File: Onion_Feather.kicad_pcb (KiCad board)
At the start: 4 copper layers, 59.7 x 53.3 mm, 65 parts, among them IC1 MAX11646EUA+T, IC2 SN74HC367PWR, J1 HR911105A, J2 CON_HEADER_PRG_AVR_ICSP-PTH, J3 Conn_01x02, J4 USB_A, J5 M04PTH, U1 ONION-OMEGA2, U2 AP1117-33, U3 CP2102N-A01-GQFN24, U4 BQ25895RTW, U5 STF202-22T1G

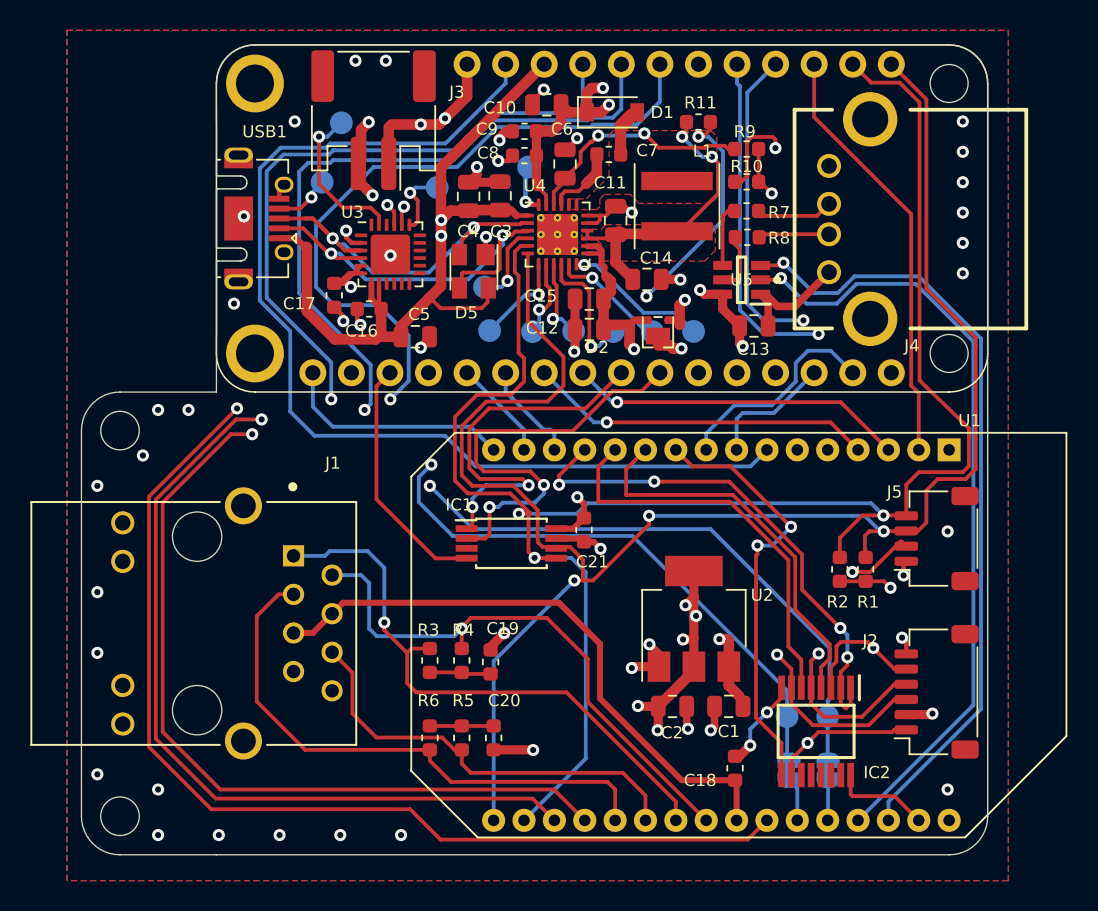
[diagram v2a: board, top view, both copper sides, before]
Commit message: #8 Re-route USB filter
Signed-off-by: Tisham Dhar <whatnickd@gmail.com>
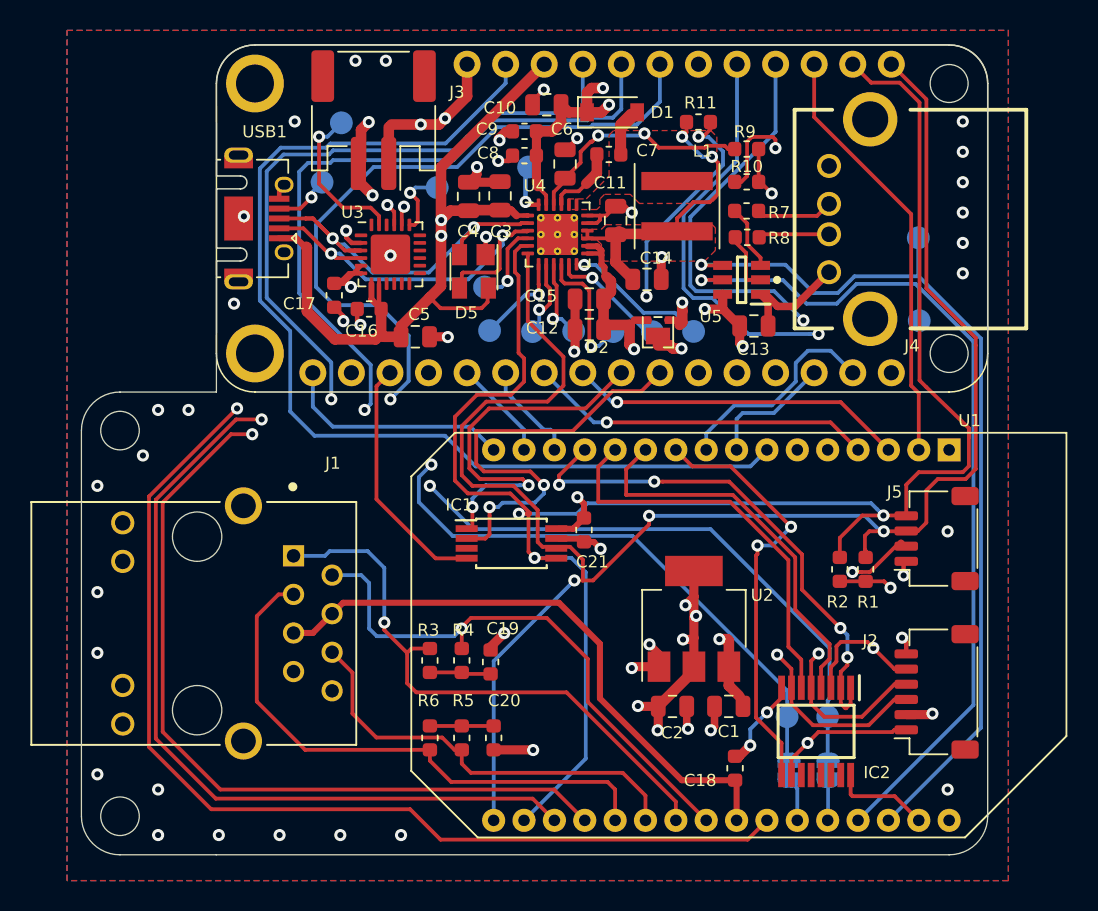
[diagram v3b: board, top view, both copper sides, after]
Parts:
- added TP14: TestPoint, TestPoint:TestPoint_Pad_D1.5mm, B.Cu at (163.1, 73.7)
- added TP15: TestPoint, TestPoint:TestPoint_Pad_D1.5mm, B.Cu at (163.1, 79.1)
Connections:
- U5 pad 2: USB_OUT- -> Net-(R8-Pad1)
- U5 pad 3: USB_OUT+ -> Net-(R7-Pad1)
- U5 pad 4: Net-(R7-Pad1) -> USB_OUT+
- U5 pad 5: Net-(R8-Pad1) -> USB_OUT-
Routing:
- net USB_OUT+: track 51.8 -> 59.6 mm
- net USB_OUT-: track 51.6 -> 59.3 mm
- net GPIO16: track 29.5 -> 34.1 mm
- net GPIO17: track 30.3 -> 34.6 mm
- net GND: track 64.0 -> 65.0 mm
- net VBAT: track 53.5 -> 52.9 mm
- net VIN: track 75.5 -> 75.0 mm

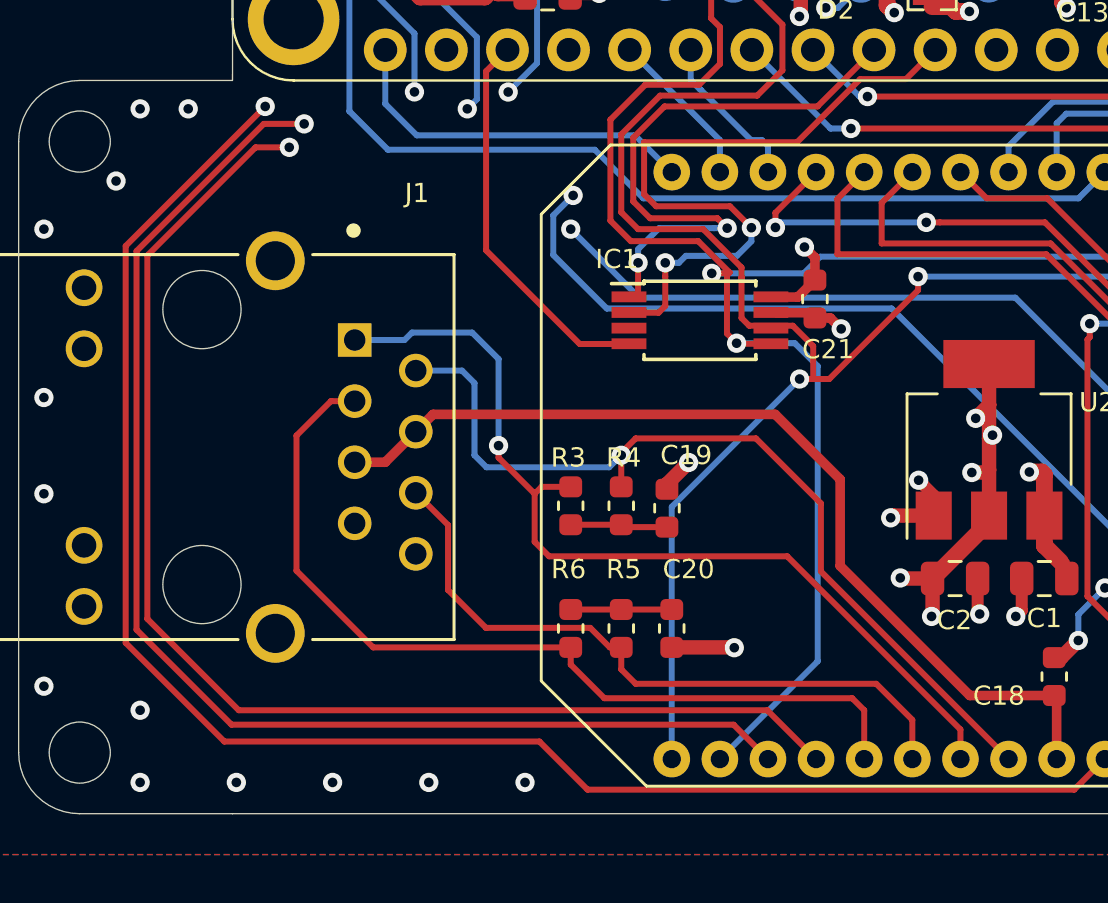
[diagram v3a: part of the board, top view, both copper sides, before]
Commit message: #9 Add some testpoints for ethernet
Signed-off-by: Tisham Dhar <whatnickd@gmail.com>
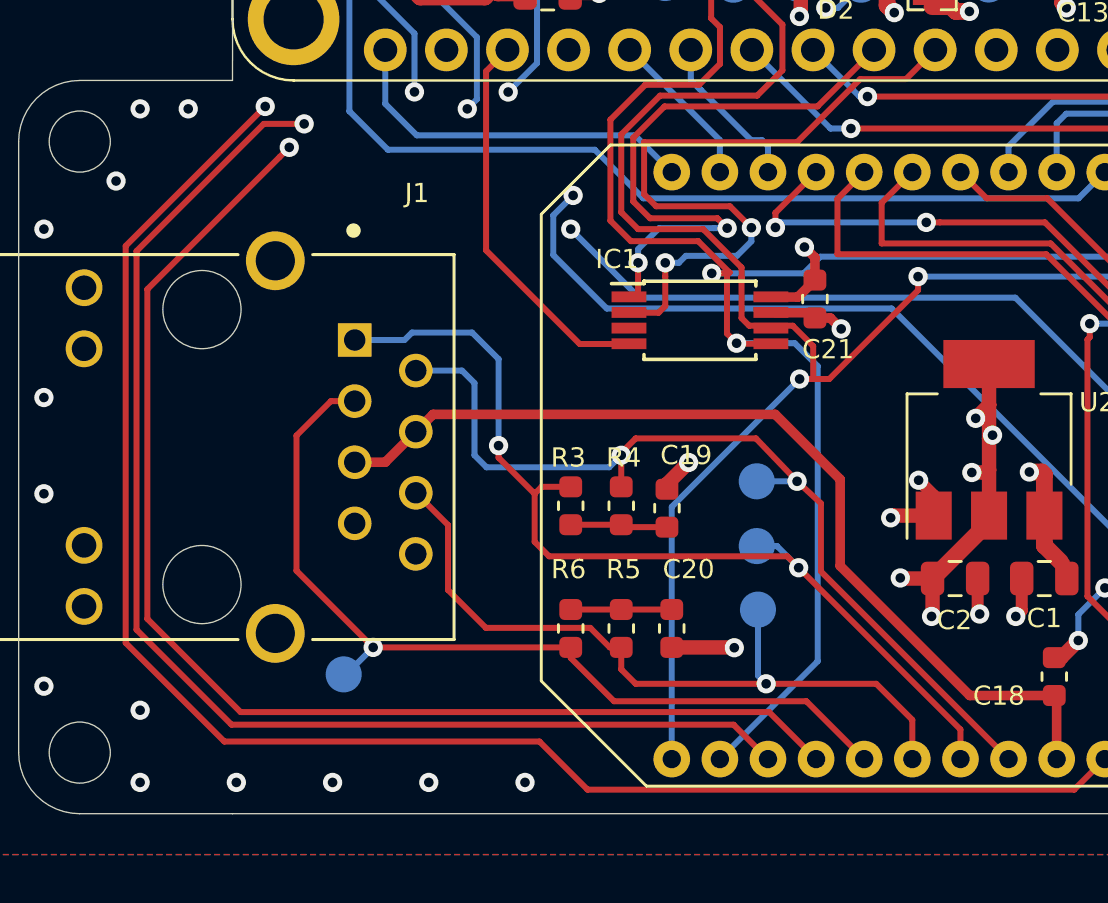
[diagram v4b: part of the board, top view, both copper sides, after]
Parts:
- added TP16: TestPoint, TestPoint:TestPoint_Pad_D1.5mm, B.Cu at (138.7, 105.8)
- added TP17: TestPoint, TestPoint:TestPoint_Pad_D1.5mm, B.Cu at (121.5, 108.5)
- added TP18: TestPoint, TestPoint:TestPoint_Pad_D1.5mm, B.Cu at (138.6, 100.5)
- added TP19: TestPoint, TestPoint:TestPoint_Pad_D1.5mm, B.Cu at (138.6, 103.2)
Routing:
- net ETH_RX-: track 28.3 -> 31.5 mm, vias 0 -> 1
- net ETH_TX+: track 38.6 -> 40.7 mm, vias 1 -> 2
- net ETH_TX-: track 37.1 -> 38.8 mm, vias 1 -> 2
- net GPIO18: track 104.8 -> 104.0 mm
- net ETH_RX+: track 37.1 -> 37.4 mm, vias 0 -> 1
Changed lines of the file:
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@@
     (thickness 1.6)
     (drawings 18)
-    (tracks 1120)
+    (tracks 1132)
     (zones 0)
-    (modules 67)
+    (modules 71)
     (nets 92)
   )
@@
   )
   (module TestPoint:TestPoint_Pad_D1.5mm (layer B.Cu)
+    (at 138.6332 103.1748)
+    (descr "SMD pad as test Point, diameter 1.5mm")
+    (tags "test point SMD pad")
+    (attr virtual)
+    (fp_text reference TP19 (at 3.4544 -0.0508) (layer B.SilkS)
+      (effects (font (size 1 1) (thickness 0.15)) (justify mirror))
+    )
+    (fp_text value TestPoint (at 0 -1.75) (layer B.Fab)
+      (effects (font (size 1 1) (thickness 0.15)) (justify mirror))
+    )
+    (fp_circle (center 0 0) (end 0 -0.95) (layer B.SilkS) (width 0.12))
+    (fp_circle (center 0 0) (end 1.25 0) (layer B.CrtYd) (width 0.05))
+    (fp_text user %R (at 0 1.65) (layer B.Fab)
+      (effects (font (size 1 1) (thickness 0.15)) (justify mirror))
+    )
+    (pad 1 smd circle (at 0 0) (size 1.5 1.5) (layers B.Cu B.Mask)
+      (net 30 ETH_TX+))
+  )
+  (module TestPoint:TestPoint_Pad_D1.5mm (layer B.Cu)
+    (at 138.6332 100.4824)
+    (descr "SMD pad as test Point, diameter 1.5mm")
+    (tags "test point SMD pad")
+    (attr virtual)
+    (fp_text reference TP18 (at 3.4036 0) (layer B.SilkS)
+      (effects (font (size 1 1) (thickness 0.15)) (justify mirror))
+    )
+    (fp_text value TestPoint (at 0 -1.75) (layer B.Fab)
+      (effects (font (size 1 1) (thickness 0.15)) (justify mirror))
+    )
+    (fp_circle (center 0 0) (end 0 -0.95) (layer B.SilkS) (width 0.12))
+    (fp_circle (center 0 0) (end 1.25 0) (layer B.CrtYd) (width 0.05))
+    (fp_text user %R (at 0 1.65) (layer B.Fab)
+      (effects (font (size 1 1) (thickness 0.15)) (justify mirror))
+    )
+    (pad 1 smd circle (at 0 0) (size 1.5 1.5) (layers B.Cu B.Mask)
+      (net 29 ETH_TX-))
+  )
+  (module TestPoint:TestPoint_Pad_D1.5mm (layer B.Cu)
+    (at 121.4628 108.5088)
+    (descr "SMD pad as test Point, diameter 1.5mm")
+    (tags "test point SMD pad")
+    (attr virtual)
+    (fp_text reference TP17 (at 0 1.648) (layer B.SilkS)
+      (effects (font (size 1 1) (thickness 0.15)) (justify mirror))
+    )
+    (fp_text value TestPoint (at 0 -1.75) (layer B.Fab)
+      (effects (font (size 1 1) (thickness 0.15)) (justify mirror))
+    )
+    (fp_circle (center 0 0) (end 0 -0.95) (layer B.SilkS) (width 0.12))
+    (fp_circle (center 0 0) (end 1.25 0) (layer B.CrtYd) (width 0.05))
+    (fp_text user %R (at 0 1.65) (layer B.Fab)
+      (effects (font (size 1 1) (thickness 0.15)) (justify mirror))
+    )
+    (pad 1 smd circle (at 0 0) (size 1.5 1.5) (layers B.Cu B.Mask)
+      (net 28 ETH_RX+))
+  )
+  (module TestPoint:TestPoint_Pad_D1.5mm (layer B.Cu)
+    (at 138.684 105.8164)
+    (descr "SMD pad as test Point, diameter 1.5mm")
+    (tags "test point SMD pad")
+    (attr virtual)
+    (fp_text reference TP16 (at 3.4544 0.1524) (layer B.SilkS)
+      (effects (font (size 1 1) (thickness 0.15)) (justify mirror))
+    )
+    (fp_text value TestPoint (at 0 -1.75) (layer B.Fab)
+      (effects (font (size 1 1) (thickness 0.15)) (justify mirror))
+    )
+    (fp_circle (center 0 0) (end 0 -0.95) (layer B.SilkS) (width 0.12))
+    (fp_circle (center 0 0) (end 1.25 0) (layer B.CrtYd) (width 0.05))
+    (fp_text user %R (at 0 1.65) (layer B.Fab)
+      (effects (font (size 1 1) (thickness 0.15)) (justify mirror))
+    )
+    (pad 1 smd circle (at 0 0) (size 1.5 1.5) (layers B.Cu B.Mask)
+      (net 27 ETH_RX-))
+  )
+  (module TestPoint:TestPoint_Pad_D1.5mm (layer B.Cu)
     (at 163.1315 79.121)
     (descr "SMD pad as test Point, diameter 1.5mm")
@@
   (segment (start 133 108.3) (end 133 107.3875) (width 0.25) (layer F.Cu) (net 27) (status 20))
   (segment (start 133.6 108.9) (end 133 108.3) (width 0.25) (layer F.Cu) (net 27))
-  (segment (start 143.1 112.03) (end 143.1 110) (width 0.25) (layer F.Cu) (net 28) (status 10))
-  (segment (start 143.1 110) (end 142.6 109.5) (width 0.25) (layer F.Cu) (net 28))
-  (segment (start 142.6 109.5) (end 132.3 109.5) (width 0.25) (layer F.Cu) (net 28))
-  (segment (start 130.9 108.1) (end 130.9 107.3875) (width 0.25) (layer F.Cu) (net 28) (status 20))
-  (segment (start 132.3 109.5) (end 130.9 108.1) (width 0.25) (layer F.Cu) (net 28))
+  (segment (start 138.684 108.5596) (end 139.0244 108.9) (width 0.25) (layer B.Cu) (net 27))
+  (segment (start 138.684 105.8164) (end 138.684 108.5596) (width 0.25) (layer B.Cu) (net 27))
+  (via (at 139.0244 108.9) (size 0.8) (drill 0.4) (layers F.Cu B.Cu) (net 27))
   (segment (start 122.6875 107.3875) (end 119.5 104.2) (width 0.25) (layer F.Cu) (net 28))
   (segment (start 130.9 107.3875) (end 122.6875 107.3875) (width 0.25) (layer F.Cu) (net 28) (status 10))
@@
   (segment (start 120.931465 97.15) (end 119.5 98.581465) (width 0.25) (layer F.Cu) (net 28))
   (segment (start 121.92 97.15) (end 120.931465 97.15) (width 0.25) (layer F.Cu) (net 28) (status 10))
+  (segment (start 132.700001 109.625001) (end 130.9 107.825) (width 0.25) (layer F.Cu) (net 28))
+  (segment (start 143.1 112.03) (end 140.695001 109.625001) (width 0.25) (layer F.Cu) (net 28))
+  (segment (start 140.695001 109.625001) (end 132.700001 109.625001) (width 0.25) (layer F.Cu) (net 28))
+  (segment (start 130.9 107.825) (end 130.9 107.3875) (width 0.25) (layer F.Cu) (net 28))
+  (via (at 122.6875 107.3875) (size 0.8) (drill 0.4) (layers F.Cu B.Cu) (net 28))
+  (segment (start 121.4628 108.5088) (end 121.5662 108.5088) (width 0.25) (layer B.Cu) (net 28))
+  (segment (start 121.5662 108.5088) (end 122.6875 107.3875) (width 0.25) (layer B.Cu) (net 28))
   (segment (start 149.1 112.03) (end 141.3 104.23) (width 0.25) (layer F.Cu) (net 29) (status 10))
   (segment (start 141.3 104.23) (end 141.3 101.4) (width 0.25) (layer F.Cu) (net 29))
-  (segment (start 141.3 101.4) (end 138.6 98.7) (width 0.25) (layer F.Cu) (net 29))
   (segment (start 138.6 98.7) (end 133.6 98.7) (width 0.25) (layer F.Cu) (net 29))
   (segment (start 133.6 98.7) (end 133 99.3) (width 0.25) (layer F.Cu) (net 29))
@@
   (segment (start 133 99.3) (end 133 99.4) (width 0.25) (layer F.Cu) (net 29))
   (segment (start 124.46 95.88) (end 126.38 95.88) (width 0.25) (layer B.Cu) (net 29) (status 10))
+  (via (at 140.3096 100.4824) (size 0.8) (drill 0.4) (layers F.Cu B.Cu) (net 29))
+  (segment (start 138.6332 100.4824) (end 140.3096 100.4824) (width 0.25) (layer B.Cu) (net 29))
+  (segment (start 141.3 101.4) (end 140.3096 100.4824) (width 0.25) (layer F.Cu) (net 29))
+  (segment (start 140.3096 100.4824) (end 138.6 98.7) (width 0.25) (layer F.Cu) (net 29))
   (segment (start 147.1 112.03) (end 147.1 110.8) (width 0.25) (layer F.Cu) (net 30) (status 10))
-  (segment (start 147.1 110.8) (end 139.9 103.6) (width 0.25) (layer F.Cu) (net 30))
   (segment (start 139.9 103.6) (end 130 103.6) (width 0.25) (layer F.Cu) (net 30))
   (segment (start 130 103.6) (end 129.4 103) (width 0.25) (layer F.Cu) (net 30))
@@
   (segment (start 123.99 94.61) (end 121.92 94.61) (width 0.25) (layer B.Cu) (net 30) (status 20))
   (segment (start 124.3 94.3) (end 123.99 94.61) (width 0.25) (layer B.Cu) (net 30))
+  (segment (start 138.6332 103.1748) (end 139.4748 103.1748) (width 0.25) (layer B.Cu) (net 30))
+  (segment (start 139.4748 103.1748) (end 140.3748 104.0748) (width 0.25) (layer B.Cu) (net 30))
+  (segment (start 147.1 110.8) (end 140.3748 104.0748) (width 0.25) (layer F.Cu) (net 30))
+  (via (at 140.3748 104.0748) (size 0.8) (drill 0.4) (layers F.Cu B.Cu) (net 30))
+  (segment (start 140.3748 104.0748) (end 139.9 103.6) (width 0.25) (layer F.Cu) (net 30))
   (segment (start 119.7 69.1) (end 121.074999 67.725001) (width 0.25) (layer B.Cu) (net 31))
   (segment (start 121.7 79.8) (end 119.7 77.8) (width 0.25) (layer B.Cu) (net 31))
@@
   (segment (start 125 86.6) (end 119.200018 86.6) (width 0.25) (layer In2.Cu) (net 33))
   (segment (start 126.6 85) (end 125 86.6) (width 0.25) (layer In2.Cu) (net 33))
-  (segment (start 117.8 86.6) (end 119.200018 86.6) (width 0.25) (layer F.Cu) (net 33))
-  (segment (start 139.07 110) (end 117.1 110) (width 0.25) (layer F.Cu) (net 33))
-  (segment (start 113.3 91.1) (end 117.8 86.6) (width 0.25) (layer F.Cu) (net 33))
-  (segment (start 141.1 112.03) (end 139.07 110) (width 0.25) (layer F.Cu) (net 33) (status 10))
-  (segment (start 117.1 110) (end 113.3 106.2) (width 0.25) (layer F.Cu) (net 33))
-  (segment (start 113.3 106.2) (end 113.3 91.1) (width 0.25) (layer F.Cu) (net 33))
   (segment (start 122.291173 69.308827) (end 122.291173 77.314451) (width 0.25) (layer B.Cu) (net 33))
   (segment (start 143.51 65.19) (end 142.946013 65.753987) (width 0.25) (layer B.Cu) (net 33))
@@
   (segment (start 143.51 62.23) (end 143.51 65.19) (width 0.25) (layer B.Cu) (net 33) (status 10))
   (segment (start 135.075011 65.924989) (end 132.450011 68.549989) (width 0.25) (layer B.Cu) (net 33))
+  (segment (start 139.145012 110.075012) (end 117.175012 110.075012) (width 0.25) (layer F.Cu) (net 33))
+  (segment (start 117.175012 110.075012) (end 113.3 106.2) (width 0.25) (layer F.Cu) (net 33))
+  (segment (start 118.800019 86.999999) (end 119.200018 86.6) (width 0.25) (layer F.Cu) (net 33))
+  (segment (start 113.3 106.2) (end 113.3 92.500018) (width 0.25) (layer F.Cu) (net 33))
+  (segment (start 113.3 92.500018) (end 118.800019 86.999999) (width 0.25) (layer F.Cu) (net 33))
+  (segment (start 141.1 112.03) (end 139.145012 110.075012) (width 0.25) (layer F.Cu) (net 33))
   (via (at 119.818987 85.625) (size 0.8) (drill 0.4) (layers F.Cu B.Cu) (net 34))
   (segment (start 119.818987 85.625) (end 124.475 85.625) (width 0.25) (layer In2.Cu) (net 34))
